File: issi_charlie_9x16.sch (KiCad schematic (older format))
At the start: 149 parts, among them U1 IS31FL3731-QF

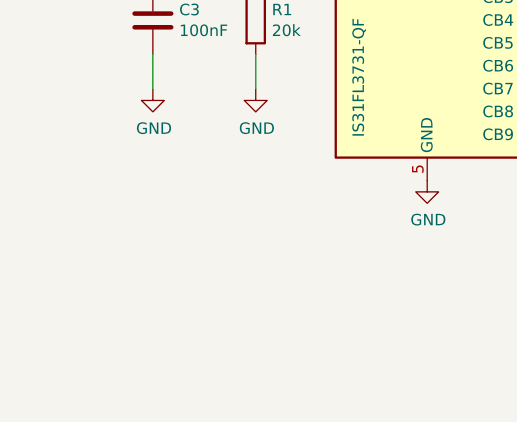
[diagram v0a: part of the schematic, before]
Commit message: Updates to production version
Changed infrared setup, added step-up for battery power, added battery power switch, added more capacitors, changed and added logos, etc.
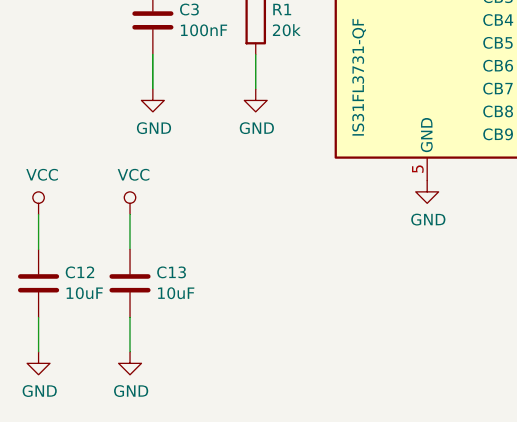
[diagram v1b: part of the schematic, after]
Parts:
- added C12, C13: 10uF, Capacitors_SMD:C_0603, symbol device:C
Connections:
- net GND: now also C12.2, C13.2
- net VCC: now also C12.1, C13.1
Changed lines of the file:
@@
 AR Path="/5EC90811/5EC967D5" Ref="#PWR010"  Part="1"
 AR Path="/5F64D6C7/5EC967D5" Ref="#PWR018"  Part="1"
-F 0 "#PWR018" H 3250 3650 50  0001 C CNN
+F 0 "#PWR010" H 3250 3650 50  0001 C CNN
 F 1 "GND" H 3255 3727 50  0000 C CNN
 F 2 "" H 3250 3900 50  0001 C CNN
@@
 AR Path="/5EC90811/5EC9ABDC" Ref="#PWR08"  Part="1"
 AR Path="/5F64D6C7/5EC9ABDC" Ref="#PWR016"  Part="1"
-F 0 "#PWR016" H 2500 3250 50  0001 C CNN
+F 0 "#PWR08" H 2500 3250 50  0001 C CNN
 F 1 "GND" H 2505 3327 50  0000 C CNN
 F 2 "" H 2500 3500 50  0001 C CNN
@@
 AR Path="/5EC90811/5EC9B121" Ref="#PWR07"  Part="1"
 AR Path="/5F64D6C7/5EC9B121" Ref="#PWR015"  Part="1"
-F 0 "#PWR015" H 2050 3250 50  0001 C CNN
+F 0 "#PWR07" H 2050 3250 50  0001 C CNN
 F 1 "GND" H 2055 3327 50  0000 C CNN
 F 2 "" H 2050 3500 50  0001 C CNN
@@
 AR Path="/5EC90811/5ECA1D26" Ref="#PWR0101"  Part="1"
 AR Path="/5F64D6C7/5ECA1D26" Ref="#PWR012"  Part="1"
-F 0 "#PWR012" H 1550 2050 50  0001 C CNN
+F 0 "#PWR0101" H 1550 2050 50  0001 C CNN
 F 1 "GND" H 1555 2127 50  0000 C CNN
 F 2 "" H 1550 2300 50  0001 C CNN
@@
 AR Path="/5EC90811/5ECA219F" Ref="#PWR06"  Part="1"
 AR Path="/5F64D6C7/5ECA219F" Ref="#PWR014"  Part="1"
-F 0 "#PWR014" H 1950 2050 50  0001 C CNN
+F 0 "#PWR06" H 1950 2050 50  0001 C CNN
 F 1 "GND" H 1955 2127 50  0000 C CNN
 F 2 "" H 1950 2300 50  0001 C CNN
@@
 AR Path="/5EC90811/5ED7C8A4" Ref="#PWR09"  Part="1"
 AR Path="/5F64D6C7/5ED7C8A4" Ref="#PWR017"  Part="1"
-F 0 "#PWR017" H 3250 1550 50  0001 C CNN
+F 0 "#PWR09" H 3250 1550 50  0001 C CNN
 F 1 "VCC" H 3267 1873 50  0000 C CNN
 F 2 "" H 3250 1700 50  0001 C CNN
@@
 AR Path="/5EC90811/5ED7D0DF" Ref="#PWR05"  Part="1"
 AR Path="/5F64D6C7/5ED7D0DF" Ref="#PWR013"  Part="1"
-F 0 "#PWR013" H 1950 1550 50  0001 C CNN
+F 0 "#PWR05" H 1950 1550 50  0001 C CNN
 F 1 "VCC" H 1967 1873 50  0000 C CNN
 F 2 "" H 1950 1700 50  0001 C CNN
@@
 AR Path="/5EC90811/5ED7D663" Ref="#PWR0102"  Part="1"
 AR Path="/5F64D6C7/5ED7D663" Ref="#PWR011"  Part="1"
-F 0 "#PWR011" H 1550 1550 50  0001 C CNN
+F 0 "#PWR0102" H 1550 1550 50  0001 C CNN
 F 1 "VCC" H 1567 1873 50  0000 C CNN
 F 2 "" H 1550 1700 50  0001 C CNN
@@
 	1    0    0    -1
 $EndComp
+$Comp
+L device:C C12
+U 1 1 5F0856E4
+P 1550 4350
+AR Path="/5EC90811/5F0856E4" Ref="C12"  Part="1"
+AR Path="/5F64D6C7/5F0856E4" Ref="C14"  Part="1"
+F 0 "C12" H 1665 4396 50  0000 L CNN
+F 1 "10uF" H 1665 4305 50  0000 L CNN
+F 2 "Capacitors_SMD:C_0603" H 1588 4200 50  0001 C CNN
+F 3 "~" H 1550 4350 50  0001 C CNN
+	1    1550 4350
+	1    0    0    -1
+$EndComp
+$Comp
+L power:GND #PWR057
+U 1 1 5F0856EA
+P 1550 4650
+AR Path="/5EC90811/5F0856EA" Ref="#PWR057"  Part="1"
+AR Path="/5F64D6C7/5F0856EA" Ref="#PWR061"  Part="1"
+F 0 "#PWR057" H 1550 4400 50  0001 C CNN
+F 1 "GND" H 1555 4477 50  0000 C CNN
+F 2 "" H 1550 4650 50  0001 C CNN
+F 3 "" H 1550 4650 50  0001 C CNN
+	1    1550 4650
+	1    0    0    -1
+$EndComp
+Wire Wire Line
+	1550 4650 1550 4500
+Wire Wire Line
+	1550 4200 1550 4050
+$Comp
+L power:VCC #PWR051
+U 1 1 5F0856F2
+P 1550 4050
+AR Path="/5EC90811/5F0856F2" Ref="#PWR051"  Part="1"
+AR Path="/5F64D6C7/5F0856F2" Ref="#PWR060"  Part="1"
+F 0 "#PWR051" H 1550 3900 50  0001 C CNN
+F 1 "VCC" H 1567 4223 50  0000 C CNN
+F 2 "" H 1550 4050 50  0001 C CNN
+F 3 "" H 1550 4050 50  0001 C CNN
+	1    1550 4050
+	1    0    0    -1
+$EndComp
+$Comp
+L device:C C13
+U 1 1 5F0C0050
+P 1950 4350
+AR Path="/5EC90811/5F0C0050" Ref="C13"  Part="1"
+AR Path="/5F64D6C7/5F0C0050" Ref="C15"  Part="1"
+F 0 "C13" H 2065 4396 50  0000 L CNN
+F 1 "10uF" H 2065 4305 50  0000 L CNN
+F 2 "Capacitors_SMD:C_0603" H 1988 4200 50  0001 C CNN
+F 3 "~" H 1950 4350 50  0001 C CNN
+	1    1950 4350
+	1    0    0    -1
+$EndComp
+$Comp
+L power:GND #PWR059
+U 1 1 5F0C0056
+P 1950 4650
+AR Path="/5EC90811/5F0C0056" Ref="#PWR059"  Part="1"
+AR Path="/5F64D6C7/5F0C0056" Ref="#PWR063"  Part="1"
+F 0 "#PWR059" H 1950 4400 50  0001 C CNN
+F 1 "GND" H 1955 4477 50  0000 C CNN
+F 2 "" H 1950 4650 50  0001 C CNN
+F 3 "" H 1950 4650 50  0001 C CNN
+	1    1950 4650
+	1    0    0    -1
+$EndComp
+Wire Wire Line
+	1950 4650 1950 4500
+Wire Wire Line
+	1950 4200 1950 4050
+$Comp
+L power:VCC #PWR058
+U 1 1 5F0C005E
+P 1950 4050
+AR Path="/5EC90811/5F0C005E" Ref="#PWR058"  Part="1"
+AR Path="/5F64D6C7/5F0C005E" Ref="#PWR062"  Part="1"
+F 0 "#PWR058" H 1950 3900 50  0001 C CNN
+F 1 "VCC" H 1967 4223 50  0000 C CNN
+F 2 "" H 1950 4050 50  0001 C CNN
+F 3 "" H 1950 4050 50  0001 C CNN
+	1    1950 4050
+	1    0    0    -1
+$EndComp
